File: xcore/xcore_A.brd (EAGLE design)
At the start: 70 x 70 mm, 37 parts, among them U1 NC7WZ07, X1 XEF216-512-TQ128

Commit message: xcore: part number for pinhead 3x21
Signed-off-by: malo <pavol.malosek@gmail.com>
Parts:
- J_TO_MASTER, J_TO_SLAVE: value PINHD-3X21/90 -> TSW-121-08-G-T-RA
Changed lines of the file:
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@@
 <attribute name="NAME" x="22.843" y="28.1356" size="1.27" layer="25"/>
 </element>
-<element name="J_TO_MASTER" library="25pinhead" package="3X21/90" value="PINHD-3X21/90" x="35" y="71.308"/>
-<element name="J_TO_SLAVE" library="25pinhead" package="3X21/90" value="PINHD-3X21/90" x="35" y="-1.3208" rot="R180"/>
+<element name="J_TO_MASTER" library="25pinhead" package="3X21/90" value="TSW-121-08-G-T-RA" x="35" y="71.308"/>
+<element name="J_TO_SLAVE" library="25pinhead" package="3X21/90" value="TSW-121-08-G-T-RA" x="35" y="-1.3208" rot="R180"/>
 </elements>
 <signals>

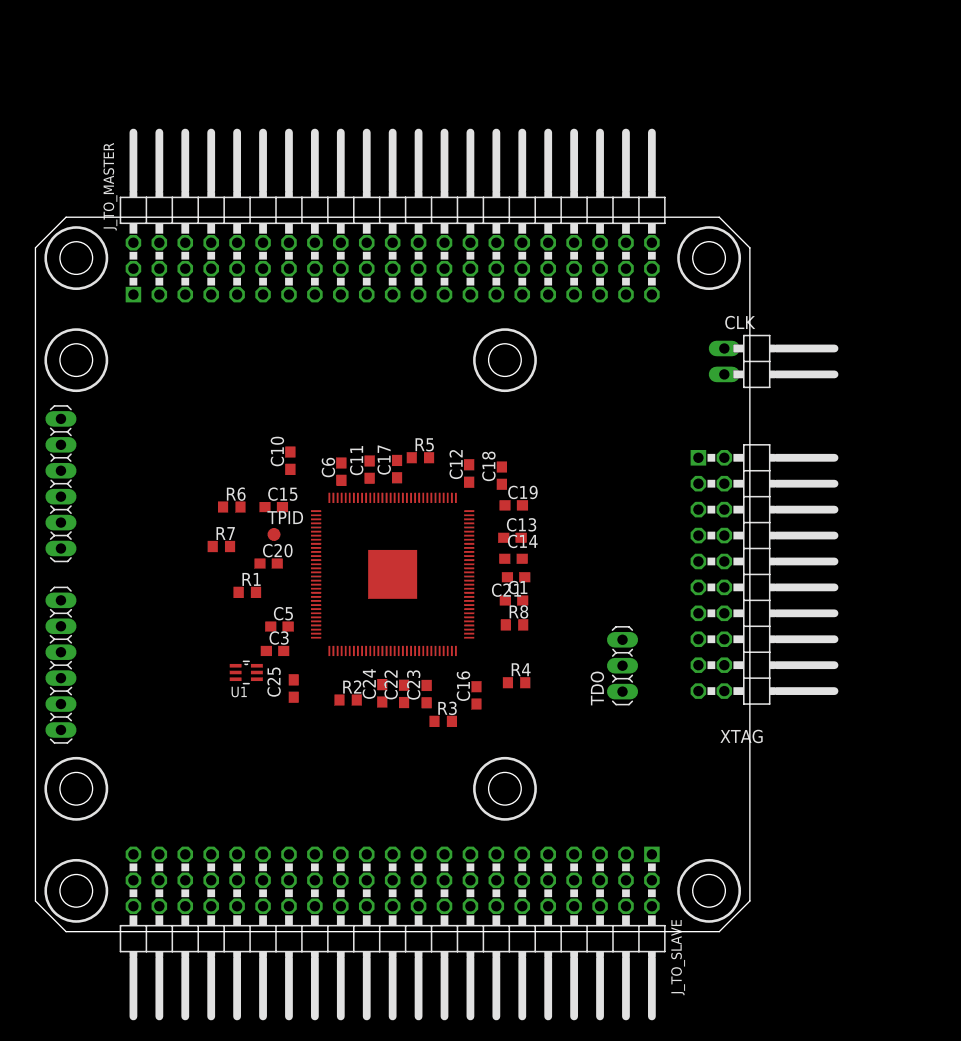
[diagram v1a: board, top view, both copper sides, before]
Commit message: xcore: updated PWR to LIWE_12_PIN_8X8_COMPAT
Signed-off-by: malo <pavol.malosek@gmail.com>
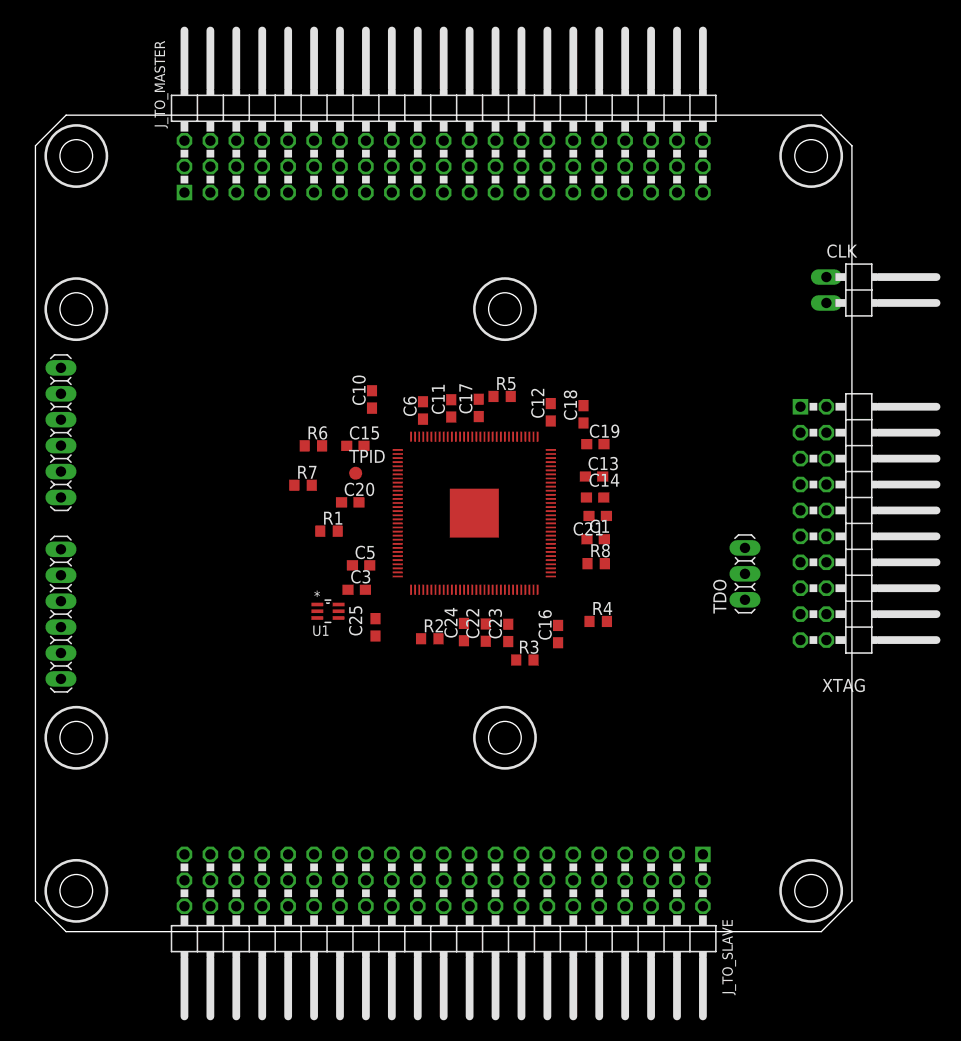
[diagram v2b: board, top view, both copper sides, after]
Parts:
- PWR: device 25cmsquare:LIWE_12_PIN_7X7_COMPAT -> 25cmsquare:LIWE_12_PIN_8X8_COMPAT
- moved TDO 15.0 mm to (69.5, 35.1)
- moved PWR 14.1 mm to (80.0, 80.0)
- moved CLK 12.2 mm to (81.3, 62.9)
- moved J_TO_MASTER 11.2 mm to (40.0, 81.3)
- moved XTAG 11.2 mm to (81.3, 40.0)
- moved C25 10.0 mm to (33.3, 29.8)
- moved R8 10.0 mm to (54.9, 36.1)
- moved C1 10.0 mm to (54.9, 38.4)
- moved C11 10.0 mm to (40.7, 51.3)
- moved C12 10.0 mm to (50.5, 50.9)
- moved C13 10.0 mm to (54.7, 44.6)
- moved C14 10.0 mm to (54.8, 42.5)
- moved C15 10.0 mm to (31.4, 47.6)
- moved C16 10.0 mm to (51.2, 29.1)
- moved C17 10.0 mm to (43.4, 51.3)
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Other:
- board size 70 x 70 mm -> 80 x 80 mm

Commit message: xcore: WIP PCB
Signed-off-by: malo <pavol.malosek@gmail.com>
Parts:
- removed C5, C6: 100n, 0603, rcl:C0603
- added C26, C27, C28: 100n, 0603, rcl:C0603K
- C10, C11, C12, C13, C14, C16, C17, C18, C22, C23, C24, C25: device rcl:C0603 -> rcl:C0603K
- CLK: device 25pinhead:1X02/90 -> 25pinhead:1X02
- J_TO_MASTER, J_TO_SLAVE: value TSW-121-08-G-T-RA -> TSW-125-08-G-T-RA; device 25pinhead:3X21/90 -> 25pinhead:3X25/90
- moved PWR 80.0 mm to (0.01, 80.0), turned to 270 degrees
- moved CLK 62.0 mm to (45.1, 12.6), turned to 90 degrees
- moved XTAG 58.4 mm to (40.0, 81.3), turned to 0 degrees
- moved J_TO_SLAVE 55.8 mm to (2.54, 40.0), flipped to the bottom, turned to 270 degrees
- moved J_TO_MASTER 55.8 mm to (77.5, 40.0), turned to 270 degrees
- moved TDO 43.5 mm to (38.9, 65.8), turned to 180 degrees
- moved U1 42.3 mm to (58.2, 61.7), turned to 180 degrees
- moved R1 35.2 mm to (54.4, 63.4), turned to 180 degrees
- moved R2 34.8 mm to (55.6, 59.1), turned to 270 degrees
- moved R4 28.2 mm to (29.1, 41.1)
- moved R3 26.7 mm to (35.4, 50.2), turned to 270 degrees
- moved C19 23.7 mm to (35.1, 34.8), turned to 270 degrees
- moved C18 23.2 mm to (36.8, 34.8), turned to 270 degrees
- moved R6 20.9 mm to (38.2, 29.8), turned to 90 degrees
- moved C21 20.3 mm to (34.8, 40.6)
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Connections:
- net N$1 renamed X0D43
- net N$11 renamed PLL_AVDD
- net N$2 renamed IO1
- net N$3 renamed X0D42
- net N$7 renamed USB_RTUNE
- new net X0D02: J_TO_SLAVE.70, X1.37
- new net X0D03: J_TO_SLAVE.72, X1.38
- new net X0D08: J_TO_SLAVE.73, X1.39
- new net X0D09: J_TO_SLAVE.75, X1.40
- new net X0D14: J_TO_MASTER.69, X1.57
- new net X0D15: X1.58
- new net X0D16: J_TO_MASTER.58, X1.68
- new net X0D17: J_TO_MASTER.57, X1.69
- new net X0D18: J_TO_MASTER.55, X1.70
- new net X0D19: J_TO_MASTER.54, X1.71
- new net X0D20: J_TO_MASTER.67, X1.59
- new net X0D21: J_TO_MASTER.66, X1.61
- new net X0D26: J_TO_MASTER.31, X1.93
- new net X0D27: J_TO_MASTER.30, X1.94
- new net X0D28: J_TO_MASTER.27, X1.96
- new net X0D29: J_TO_MASTER.24, X1.98
- new net X0D30: J_TO_MASTER.22, X1.99
- new net X0D31: J_TO_MASTER.21, X1.100
- new net X0D32: J_TO_MASTER.28, X1.95
- new net X0D33: J_TO_MASTER.25, X1.97
- new net X1D02: J_TO_MASTER.52, X1.72
- new net X1D03: J_TO_MASTER.51, X1.74
- new net X1D04: J_TO_MASTER.49, X1.75
- new net X1D05: J_TO_MASTER.48, X1.76
- new net X1D06: J_TO_MASTER.46, X1.77
- new net X1D07: J_TO_MASTER.45, X1.79
- new net X1D08: J_TO_MASTER.43, X1.82
- new net X1D09: J_TO_MASTER.42, X1.84
- new net X1D14: J_TO_MASTER.75, X1.51
- new net X1D15: J_TO_MASTER.73, X1.53
- new net X1D16: J_TO_SLAVE.52, X1.22
- new net X1D17: J_TO_SLAVE.54, X1.23
- new net X1D18: J_TO_SLAVE.55, X1.25
- new net X1D19: J_TO_SLAVE.57, X1.26
- new net X1D20: J_TO_MASTER.72, X1.54
- new net X1D21: J_TO_MASTER.70, X1.55
- new net X1D26: J_TO_MASTER.13, X1.112
- new net X1D27: J_TO_MASTER.12, X1.113
- new net X1D28: J_TO_MASTER.10, X1.114
- new net X1D29: J_TO_MASTER.9, X1.115
- new net X1D30: J_TO_SLAVE.30, X1.116
- new net X1D31: J_TO_SLAVE.31, X1.117
- new net X1D32: J_TO_SLAVE.33, X1.118
- new net X1D33: J_TO_SLAVE.34, X1.119
- new net X1D40: J_TO_MASTER.19, X1.106
- new net X1D41: J_TO_MASTER.18, X1.107
- new net X1D42: J_TO_MASTER.16, X1.108
- new net X1D43: J_TO_MASTER.15, X1.109
- net +3V3: now also C26.2, C27.2, C28.2; no longer C5.2, C6.2
- net GND: now also C26.1, C27.1, C28.1, J_TO_MASTER.65, J_TO_MASTER.68, J_TO_MASTER.71, J_TO_MASTER.74, J_TO_SLAVE.65, J_TO_SLAVE.68, J_TO_SLAVE.71, J_TO_SLAVE.74; no longer C5.1, C6.1
- net TCK: now also J_TO_MASTER.6, J_TO_SLAVE.6; no longer J_TO_MASTER.60, J_TO_SLAVE.60
- net TDI: now also J_TO_MASTER.1, J_TO_SLAVE.1; no longer J_TO_MASTER.51, J_TO_SLAVE.51
- net TDO_IN: now also J_TO_SLAVE.3; no longer J_TO_SLAVE.54
- net TDO_OUT: now also J_TO_MASTER.3; no longer J_TO_MASTER.54
- net TMS: now also J_TO_MASTER.4, J_TO_SLAVE.4; no longer J_TO_MASTER.57, J_TO_SLAVE.57
- net X0D00: now also J_TO_SLAVE.61; no longer J_TO_MASTER.1
- net X0D01: now also J_TO_SLAVE.58; no longer J_TO_MASTER.4
- net X0D04: now also J_TO_SLAVE.63; no longer J_TO_MASTER.12
- net X0D05: now also J_TO_SLAVE.66; no longer J_TO_MASTER.15
- net X0D06: now also J_TO_SLAVE.67; no longer J_TO_MASTER.18
- net X0D07: now also J_TO_SLAVE.69; no longer J_TO_MASTER.21
- net X0D10: now also J_TO_SLAVE.60; no longer J_TO_MASTER.7
- net X0D11: now also J_TO_SLAVE.64; no longer J_TO_MASTER.10
- net X0D12: now also J_TO_MASTER.64; no longer J_TO_MASTER.13
- net X0D13: now also J_TO_MASTER.63; no longer J_TO_MASTER.16
- net X0D22: now also J_TO_MASTER.61; no longer J_TO_MASTER.19
- net X0D23: now also J_TO_MASTER.60; no longer J_TO_MASTER.22
- net X0D24: now also J_TO_MASTER.37; no longer J_TO_MASTER.25
- net X0D25: now also J_TO_MASTER.36; no longer J_TO_MASTER.28
- net X0D34: now also J_TO_MASTER.34; no longer J_TO_MASTER.31
- net X0D35: now also J_TO_MASTER.33; no longer J_TO_MASTER.34
- net X0D36: now also J_TO_SLAVE.39; no longer J_TO_MASTER.37
- net X0D37: now also J_TO_SLAVE.40; no longer J_TO_MASTER.3
- net X0D38: now also J_TO_SLAVE.42; no longer J_TO_MASTER.6
- net X0D39: now also J_TO_SLAVE.43; no longer J_TO_MASTER.9
- net X1D00: now also J_TO_MASTER.40; no longer J_TO_SLAVE.1
- net X1D01: now also J_TO_MASTER.39; no longer J_TO_SLAVE.4
- net X1D10: now also J_TO_SLAVE.36; no longer J_TO_SLAVE.7
- net X1D11: now also J_TO_SLAVE.37; no longer J_TO_SLAVE.10
- net X1D35: now also J_TO_SLAVE.45; no longer J_TO_SLAVE.13
- net X1D36: now also J_TO_SLAVE.46; no longer J_TO_SLAVE.16
- net X1D37: now also J_TO_SLAVE.48; no longer J_TO_SLAVE.19
- net X1D38: now also J_TO_SLAVE.49; no longer J_TO_SLAVE.22, J_TO_SLAVE.25
- net X1D39: now also J_TO_SLAVE.51
- net XSYS_RST_N: now also J_TO_MASTER.7, J_TO_SLAVE.7; no longer J_TO_MASTER.63, J_TO_SLAVE.63
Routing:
- net TCK: track 0.00 -> 104.1 mm
- net TDI: track 0.00 -> 83.7 mm
- net TMS: track 0.00 -> 75.4 mm
- net X0D09: track 0.00 -> 49.6 mm
- net X1D14: track 0.00 -> 49.6 mm
- net X1D20: track 0.00 -> 46.6 mm
- net X0D03: track 0.00 -> 46.2 mm
- net X0D14: track 0.00 -> 43.7 mm
- net X0D07: track 0.00 -> 43.0 mm
- net X1D15: track 0.00 -> 42.2 mm
- net TDO_OUT: track 0.00 -> 42.1 mm
- net X0D08: track 0.00 -> 42.0 mm
- net X0D21: track 0.00 -> 40.9 mm
- net X0D05: track 0.00 -> 39.7 mm
- net X1D21: track 0.00 -> 39.6 mm
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
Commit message: xcore: WIP PCB
Signed-off-by: malo <pavol.malosek@gmail.com>
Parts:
- added JP1, JP2: (no value), 25pinhead:1X03
- C10, C11, C12, C13, C14, C16, C17, C18, C22, C23, C24, C25, C26, C27, C28: device rcl:C0603K -> rcl:C0402K
- C15, C19, C20, C21, C3: device rcl:C0603 -> rcl:C0402K
- moved R2 6.72 mm to (49.5, 61.8)
- moved U1 5.61 mm to (52.7, 62.6)
- moved TPID 3.63 mm to (36.0, 29.1)
- moved R1 1.87 mm to (55.9, 62.4), turned to 270 degrees
- moved CLK 1.63 mm to (43.8, 11.5), turned to 180 degrees
- moved TDO 1.53 mm to (40.1, 66.7), turned to 270 degrees
- moved C23 1.52 mm to (43.6, 41.0), flipped to the bottom, turned to 180 degrees
- moved C24 1.50 mm to (43.6, 38.7), flipped to the bottom, turned to 180 degrees
- moved C12 0.73 mm to (44.1, 44.9), flipped to the bottom
- moved R8 0.72 mm to (45.5, 50.9), turned to 270 degrees
- moved C25 0.62 mm to (44.8, 35.6), flipped to the bottom, turned to 180 degrees
- moved C10 0.58 mm to (34.8, 44.8), flipped to the bottom
- moved C1 0.57 mm to (43.5, 50.9), turned to 270 degrees
- moved C11 0.53 mm to (37.0, 44.8), flipped to the bottom
- moved R5 0.48 mm to (28.6, 43.2)
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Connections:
- net X0D12: now also J_TO_MASTER.63; no longer J_TO_MASTER.64
- net X0D13: now also J_TO_MASTER.61; no longer J_TO_MASTER.63
- net X0D15: now also J_TO_MASTER.67
- net X0D16: now also J_TO_MASTER.57; no longer J_TO_MASTER.58
- net X0D17: now also J_TO_MASTER.55; no longer J_TO_MASTER.57
- net X0D18: now also J_TO_MASTER.54; no longer J_TO_MASTER.55
- net X0D19: now also J_TO_MASTER.52; no longer J_TO_MASTER.54
- net X0D20: now also J_TO_MASTER.66; no longer J_TO_MASTER.67
- net X0D21: now also J_TO_MASTER.64; no longer J_TO_MASTER.66
- net X0D22: now also J_TO_MASTER.60; no longer J_TO_MASTER.61
- net X0D23: now also J_TO_MASTER.58; no longer J_TO_MASTER.60
- net X0D24: now also J_TO_MASTER.36; no longer J_TO_MASTER.37
- net X0D25: now also J_TO_MASTER.34; no longer J_TO_MASTER.36
- net X0D26: now also J_TO_MASTER.30; no longer J_TO_MASTER.31
- net X0D27: now also J_TO_MASTER.28; no longer J_TO_MASTER.30
- net X0D28: now also J_TO_MASTER.25; no longer J_TO_MASTER.27
- net X0D29: now also J_TO_MASTER.22; no longer J_TO_MASTER.24
- net X0D30: now also J_TO_MASTER.21; no longer J_TO_MASTER.22
- net X0D31: now also J_TO_MASTER.19; no longer J_TO_MASTER.21
- net X0D32: now also J_TO_MASTER.27; no longer J_TO_MASTER.28
- net X0D33: now also J_TO_MASTER.24; no longer J_TO_MASTER.25
- net X0D34: now also J_TO_MASTER.33; no longer J_TO_MASTER.34
- net X0D35: now also J_TO_MASTER.31; no longer J_TO_MASTER.33
- net X1D00: now also J_TO_MASTER.39; no longer J_TO_MASTER.40
- net X1D01: now also J_TO_MASTER.37; no longer J_TO_MASTER.39
- net X1D02: now also J_TO_MASTER.51; no longer J_TO_MASTER.52
- net X1D03: now also J_TO_MASTER.49; no longer J_TO_MASTER.51
- net X1D04: now also J_TO_MASTER.48; no longer J_TO_MASTER.49
- net X1D05: now also J_TO_MASTER.46; no longer J_TO_MASTER.48
- net X1D06: now also J_TO_MASTER.45; no longer J_TO_MASTER.46
- net X1D07: now also J_TO_MASTER.43; no longer J_TO_MASTER.45
- net X1D08: now also J_TO_MASTER.42; no longer J_TO_MASTER.43
- net X1D09: now also J_TO_MASTER.40; no longer J_TO_MASTER.42
- net X1D26: now also J_TO_SLAVE.24; no longer J_TO_MASTER.13
- net X1D27: now also J_TO_SLAVE.25; no longer J_TO_MASTER.12
- net X1D28: now also J_TO_SLAVE.27; no longer J_TO_MASTER.10
- net X1D29: now also J_TO_SLAVE.28; no longer J_TO_MASTER.9
- net X1D40: now also J_TO_SLAVE.18; no longer J_TO_MASTER.19
- net X1D41: now also J_TO_SLAVE.19; no longer J_TO_MASTER.18
- net X1D42: now also J_TO_SLAVE.21; no longer J_TO_MASTER.16
- net X1D43: now also J_TO_SLAVE.22; no longer J_TO_MASTER.15
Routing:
- net +3V3: track 0.00 -> 123.7 mm, vias 0 -> 3
- net +1V0: track 0.00 -> 60.8 mm, vias 0 -> 6
- net POR: track 0.00 -> 59.5 mm, vias 0 -> 1
- net XSYS_RST_N: track 26.0 -> 80.9 mm, vias 0 -> 1
- net CLK: track 0.00 -> 54.8 mm, vias 0 -> 1
- net X1D40: track 0.00 -> 48.0 mm
- net X1D42: track 0.00 -> 47.3 mm
- net X1D26: track 0.00 -> 46.4 mm
- net X1D28: track 0.00 -> 45.9 mm
- net X1D30: track 0.00 -> 45.3 mm
- net X1D32: track 0.00 -> 44.8 mm
- net X1D10: track 0.00 -> 43.8 mm
- net X1D41: track 0.00 -> 42.0 mm
- net X1D43: track 0.00 -> 41.5 mm
- net X1D27: track 0.00 -> 40.6 mm
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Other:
- board text added: "003|002"
- board text added: "004|000"
- board text added: "005|011"
- board text added: "007|006"
- board text added: "010|001"
- board text added: "013|012"
- board text added: "015|014"
- board text added: "017|016"
- board text added: "019|018"
- board text added: "021|020"
- board text added: "023|022"
- board text added: "025|024"
- board text added: "027|026"
- board text added: "028|032"
- board text added: "029|033"
- board text added: "031|030"
- board text added: "035|034"
- board text added: "036|111"
- board text added: "038|037"
- board text added: "101|100"
- board text added: "103|102"
- board text added: "105|104"
- board text added: "107|106"
- board text added: "109|108"
- board text added: "110|133"
- board text added: "115|114"
- board text added: "117|116"
- board text added: "119|118"
- board text added: "121|120"
- board text added: "126|143"
- board text added: "128|127"
- board text added: "130|129"
- board text added: "132|131"
- board text added: "135|039"
- board text added: "137|136"
- board text added: "139|138"
- board text added: "140|"
- board text added: "142|141"
- board text added: "1V0"
- board text added: "2V5"
- board text added: "3V3"
- board text added: "5V0"
- board text added: "CLK"
- board text added: "DN"
- board text added: "DP"
- board text added: "POR"
- board text added: "TCK|TMS"
- board text added: "TDI|TDO_OUT"
- board text added: "TDO_IN|TDI"
- board text added: "TMS|TCK"
- board text added: "XSYS_RST|"
- board text added: "|XSYS_RST"

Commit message: xcore: WIP PCB
Signed-off-by: malo <pavol.malosek@gmail.com>
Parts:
- removed C24, C25, C26, C27, C28: 100n, 0603, rcl:C0402K
- removed JP1, JP2: (no value), 25pinhead:1X03
- added C31, C33, C34, C35, C36, C37, C38: 100n, 0402, rcl:C0402K
- C10, C11, C12, C13, C14, C15, C16, C17, C18, C19, C20, C21, C22, C32: value 100n, 0603 -> 100n, 0402
- XTAG: device 25pinhead:2X10/90 -> 25pinhead:2X10
- moved C22 8.01 mm to (35.4, 42.1), turned to 0 degrees
- moved XTAG 5.08 mm to (40.0, 76.2)
- moved R6 0.97 mm to (38.2, 28.9)
- moved R7 0.97 mm to (40.3, 28.9)
- moved C17 0.47 mm to (40.1, 35.2)
- moved C18 0.46 mm to (37.0, 35.2)
- moved C19 0.44 mm to (35.0, 35.2)
- moved C16 0.42 mm to (42.8, 35.2)
- moved C21 0.28 mm to (35.1, 40.8)
- moved C3 0.25 mm to (40.3, 45.3)
- moved C20 0.05 mm to (34.8, 37.5)
- renumbered C23 to C32
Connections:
- net +1V0: now also C22.2
- net +3V3: now also C31.2, C33.2, C34.2, C35.2, C36.2, C37.2, C38.2; no longer C22.2, C24.2, C25.2, C26.2, C27.2, C28.2
- net GND: now also C31.1, C33.1, C34.1, C35.1, C36.1, C37.1, C38.1; no longer C24.1, C25.1, C26.1, C27.1, C28.1
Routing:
- net +3V3: track 123.7 -> 147.1 mm, vias 3 -> 9
- net +1V0: track 60.8 -> 81.0 mm, vias 6 -> 14
- net USB_RTUNE: track 1.99 -> 2.96 mm
- net USB_VBUS: track 2.00 -> 2.96 mm
- added copper zone on layer 16, net GND

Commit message: xcore: updated with liwe 40 8x8 device
Signed-off-by: malo <pavol.malosek@gmail.com>
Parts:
- removed PWR: (no value), 25cmsquare:LIWE_12_PIN_8X8_COMPAT
- added J0: LIWE_40_PIN, 25cmsquare:LIWE_40_PIN_8X8
- moved CLK 1.90 mm to (43.8, 13.4)
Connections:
- net +1V0: now also J0.13; no longer PWR.2
- net +2V5: now also J0.15; no longer PWR.1
- net +3V3: now also J0.17; no longer PWR.4
- net +5V: now also J0.19; no longer PWR.6
- net GND: now also J0.14, J0.16, J0.18, J0.20; no longer PWR.3, PWR.8
- net IO1: now also J0.101; no longer PWR.5
- net POR: now also J0.109; no longer PWR.7
- net SCL: now also J0.105; no longer PWR.11
- net SDA: now also J0.106; no longer PWR.12
- net USB_DN: now also J0.119; no longer PWR.9
- net USB_DP: now also J0.120; no longer PWR.10
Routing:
- net +3V3: track 147.1 -> 130.9 mm
- net POR: track 59.5 -> 50.8 mm
- net USB_DN: track 32.9 -> 25.1 mm
- net USB_DP: track 33.8 -> 26.6 mm
- net IO1: track 9.00 -> 1.91 mm
- net CLK: track 54.8 -> 53.5 mm
